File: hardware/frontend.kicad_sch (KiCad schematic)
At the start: 47 parts, among them J201 Conn_01x02, J202 Conn_01x02, J203 Conn_01x02, J204 Conn_01x02, J205 Conn_01x02, Q201 NPN, Q202 2N7002, U201 BQ7694204

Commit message: update schematics
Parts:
- removed R211: 1m, Resistor_SMD:R_1206_3216Metric, symbol Device:R_Small
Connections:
- net GND: no longer C204.2, C209.2, R212.2
- net PGND renamed PACK-
- net PACK-: now also C204.2
- new net BAT-: C209.2, R212.2
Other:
- note removed: "<-- Current --"

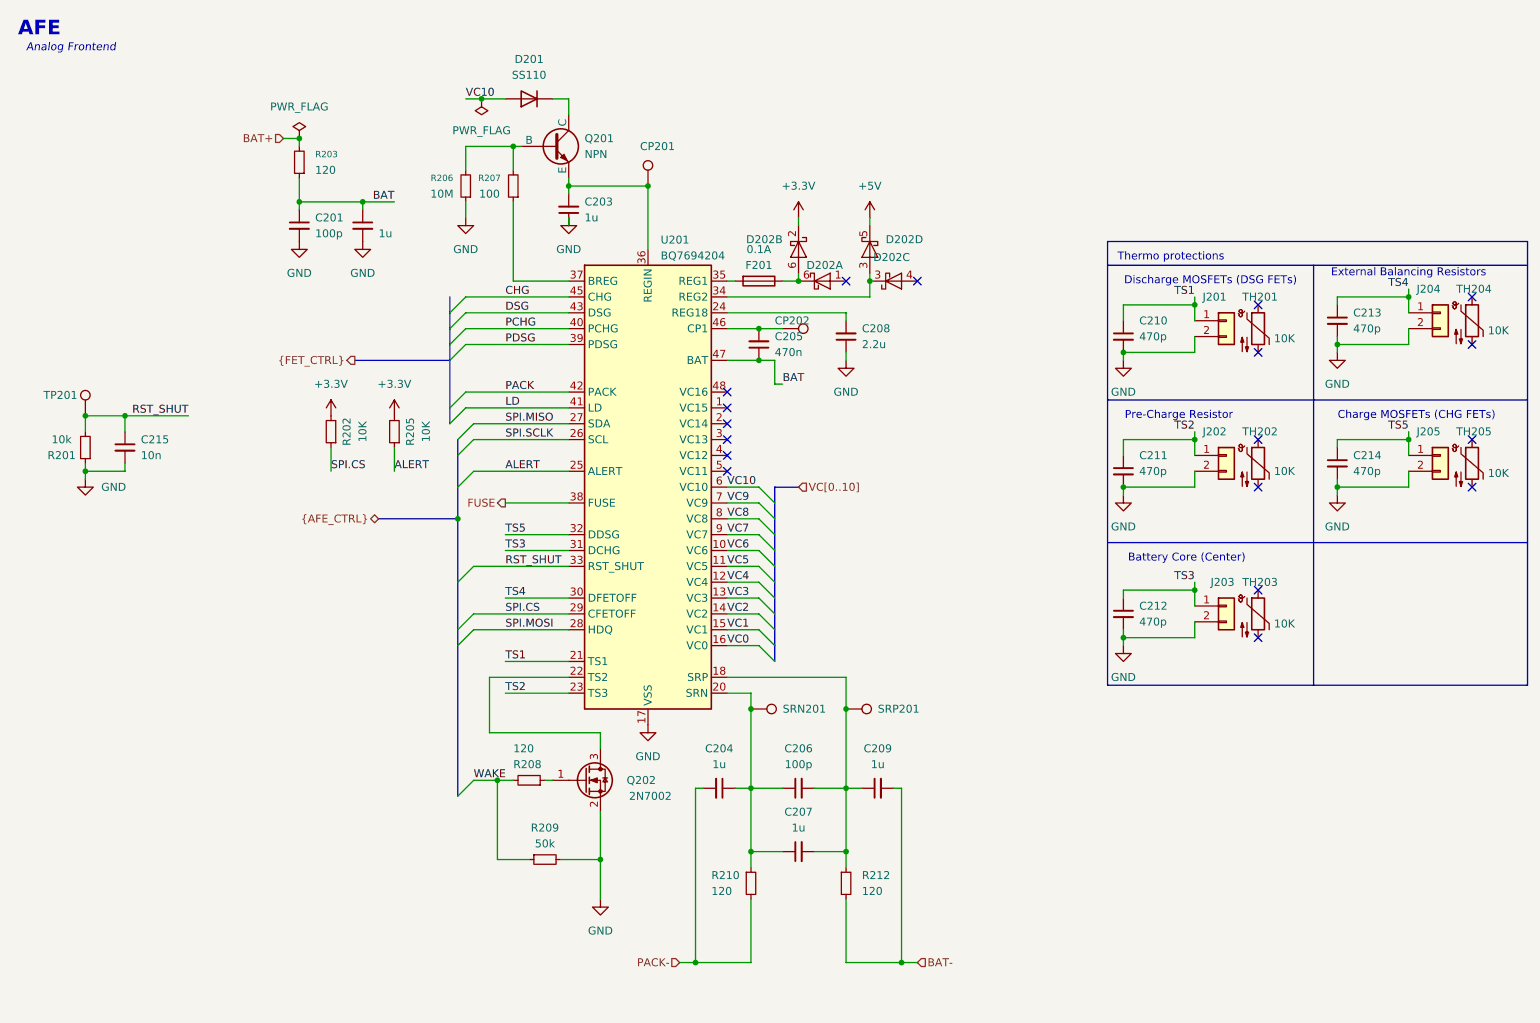
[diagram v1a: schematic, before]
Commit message: placed c mosfet
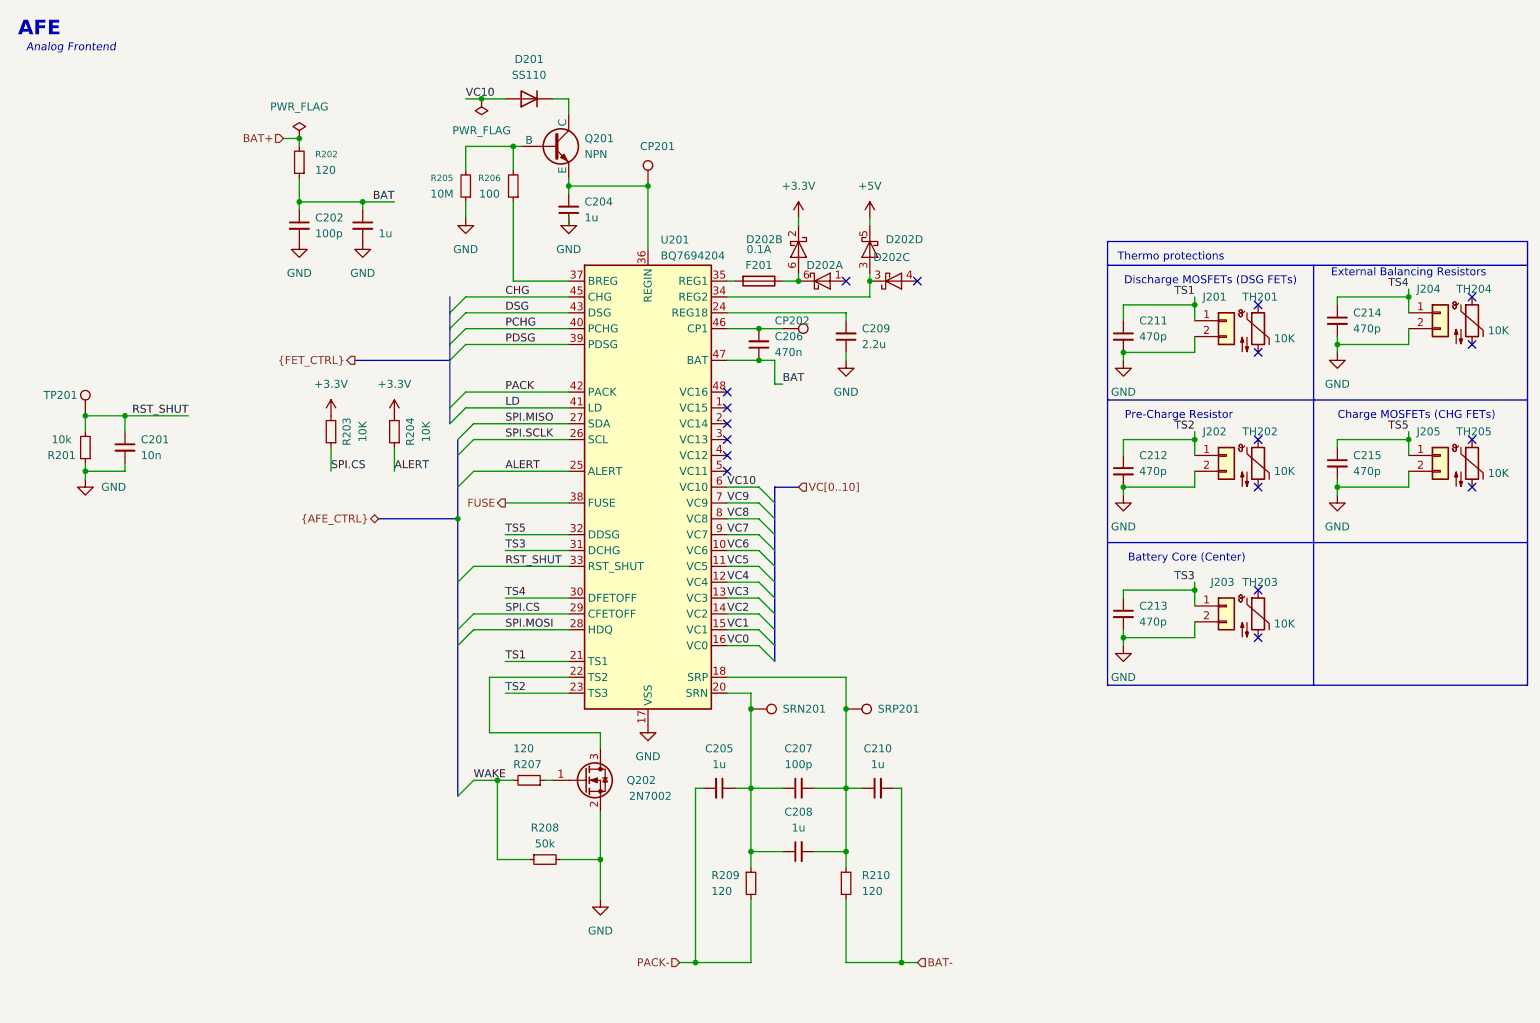
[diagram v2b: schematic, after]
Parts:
- C202: renamed from C201; footprint Capacitor_SMD:C_0805_2012Metric -> Capacitor_SMD:C_0603_1608Metric
- C204: renamed from C203; footprint Capacitor_SMD:C_0805_2012Metric -> Capacitor_SMD:C_0603_1608Metric
- C205: renamed from C204; footprint Capacitor_SMD:C_0805_2012Metric -> Capacitor_SMD:C_0603_1608Metric
- C206: renamed from C205; footprint Capacitor_SMD:C_0805_2012Metric -> Capacitor_SMD:C_0603_1608Metric
- C207: renamed from C206; footprint Capacitor_SMD:C_0805_2012Metric -> Capacitor_SMD:C_0603_1608Metric
- C208: renamed from C207; footprint Capacitor_SMD:C_0805_2012Metric -> Capacitor_SMD:C_0603_1608Metric
- C210: renamed from C209; footprint Capacitor_SMD:C_0805_2012Metric -> Capacitor_SMD:C_0603_1608Metric
- C211: renamed from C210; footprint Capacitor_SMD:C_0805_2012Metric -> Capacitor_SMD:C_0603_1608Metric
- C212: renamed from C211; footprint Capacitor_SMD:C_0805_2012Metric -> Capacitor_SMD:C_0603_1608Metric
- C213: renamed from C212; footprint Capacitor_SMD:C_0805_2012Metric -> Capacitor_SMD:C_0603_1608Metric
- C214: renamed from C213; footprint Capacitor_SMD:C_0805_2012Metric -> Capacitor_SMD:C_0603_1608Metric
- C215: renamed from C214; footprint Capacitor_SMD:C_0805_2012Metric -> Capacitor_SMD:C_0603_1608Metric
- R201: footprint Resistor_SMD:R_0805_2012Metric -> Resistor_SMD:R_0603_1608Metric
- R202: renamed from R203; footprint Resistor_SMD:R_0805_2012Metric -> Resistor_SMD:R_0603_1608Metric
- R203: renamed from R202; footprint Resistor_SMD:R_0805_2012Metric -> Resistor_SMD:R_0603_1608Metric
- R204: renamed from R205; footprint Resistor_SMD:R_0805_2012Metric -> Resistor_SMD:R_0603_1608Metric
- R205: renamed from R206; footprint Resistor_SMD:R_0805_2012Metric -> Resistor_SMD:R_0603_1608Metric
- R206: renamed from R207; footprint Resistor_SMD:R_0805_2012Metric -> Resistor_SMD:R_0603_1608Metric
- R207: renamed from R208; footprint Resistor_SMD:R_0805_2012Metric -> Resistor_SMD:R_0603_1608Metric
- R208: renamed from R209; footprint Resistor_SMD:R_0805_2012Metric -> Resistor_SMD:R_0603_1608Metric
- R209: renamed from R210; footprint Resistor_SMD:R_0805_2012Metric -> Resistor_SMD:R_0603_1608Metric
- R210: renamed from R212; footprint Resistor_SMD:R_0805_2012Metric -> Resistor_SMD:R_0603_1608Metric
- renumbered C215 to C201, C202 to C203, C208 to C209

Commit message: reduced BOM
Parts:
- C201: footprint (none) -> Capacitor_SMD:C_0603_1608Metric
- J201, J202, J203, J204, J205: footprint (none) -> Connector_Wire:SolderWire-0.15sqmm_1x02_P4mm_D0.5mm_OD1.5mm
- Q202: value 2N7002 -> DMG2302UK
- R203, R204: value 10K -> 10k
- R208: value 50k -> 49.9k
- TH201, TH202, TH203, TH204, TH205: value 10K -> 10k; footprint (none) -> Resistor_SMD:R_0603_1608Metric

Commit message: ADD ZONES
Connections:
- net BAT+ is gone; now on net VC10: R202.2
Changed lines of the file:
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@@
+	)
+	(junction
+		(at 35.56 83.82)
+		(diameter 0)
+		(color 0 0 0 0)
+	)
+	(junction
+		(at 143.51 62.23)
+		(diameter 0)
+		(color 0 0 0 0)
+	)
+	(junction
+		(at 207.01 66.04)
+		(diameter 0)
+		(color 0 0 0 0)
+	)
+	(junction
+		(at 195.58 73.66)
+		(diameter 0)
+		(color 0 0 0 0)
+	)
+	(junction
+		(at 135.89 143.51)
+		(diameter 0)
+		(color 0 0 0 0)
+	)
+	(junction
+		(at 241.3 87.63)
+		(diameter 0)
+		(color 0 0 0 0)
+	)
+	(junction
+		(at 195.58 95.25)
+		(diameter 0)
+		(color 0 0 0 0)
+	)
+	(junction
+		(at 97.79 40.64)
+		(diameter 0)
+		(color 0 0 0 0)
 	)
 	(junction
@@
 	)
 	(junction
-		(at 35.56 83.82)
-		(diameter 0)
-		(color 0 0 0 0)
-	)
-	(junction
-		(at 143.51 62.23)
-		(diameter 0)
-		(color 0 0 0 0)
-	)
-	(junction
-		(at 207.01 66.04)
-		(diameter 0)
-		(color 0 0 0 0)
-	)
-	(junction
-		(at 195.58 73.66)
-		(diameter 0)
-		(color 0 0 0 0)
-	)
-	(junction
-		(at 135.89 143.51)
-		(diameter 0)
-		(color 0 0 0 0)
-	)
-	(junction
-		(at 241.3 87.63)
-		(diameter 0)
-		(color 0 0 0 0)
-	)
-	(junction
-		(at 195.58 95.25)
-		(diameter 0)
-		(color 0 0 0 0)
-	)
-	(junction
-		(at 97.79 40.64)
-		(diameter 0)
-		(color 0 0 0 0)
-	)
-	(junction
 		(at 106.68 46.99)
 		(diameter 0)
@@
 	(wire
 		(pts
-			(xy 60.96 39.37) (xy 63.5 39.37)
+			(xy 57.15 39.37) (xy 63.5 39.37)
 		)
 		(stroke
@@
 	(label "VC7"
 		(at 132.08 102.87 0)
+		(effects
+			(font
+				(size 1.27 1.27)
+			)
+			(justify left bottom)
+		)
+	)
+	(label "VC10"
+		(at 57.15 39.37 0)
 		(effects
 			(font
@@
 		)
 	)
-	(hierarchical_label "BAT+"
-		(shape input)
-		(at 60.96 39.37 180)
-		(effects
-			(font
-				(size 1.27 1.27)
-			)
-			(justify right)
-		)
-	)

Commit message: some chnages
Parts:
- Q202: value DMG2302UK -> 2N7002K

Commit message: Replace huge SolderWire footprint with standard 2.54mm PinHeader
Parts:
- removed SRN201, SRP201: TestPoint, TestPoint:TestPoint_Pad_D1.0mm, symbol Connector:TestPoint
- J201, J202, J203, J204, J205: footprint Connector_Wire:SolderWire-0.15sqmm_1x02_P4mm_D0.5mm_OD1.5mm -> Connector_PinHeader_2.54mm:PinHeader_1x02_P2.54mm_Vertical
- TH201, TH202, TH203, TH204, TH205: now left out of the parts list
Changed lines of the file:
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@@
 	)
 	(junction
-		(at 151.13 130.81)
-		(diameter 0)
-		(color 0 0 0 0)
-	)
-	(junction
 		(at 137.16 69.85)
 		(diameter 0)
@@
 	)
 	(junction
-		(at 135.89 130.81)
-		(diameter 0)
-		(color 0 0 0 0)
-	)
-	(junction
 		(at 154.94 62.23)
 		(diameter 0)
@@
 		)
 	)
-	(wire
-		(pts
-			(xy 135.89 128.27) (xy 135.89 130.81)
-		)
-		(stroke
-			(width 0)
-			(type default)
-		)
-	)
 	(polyline
 		(pts
@@
 	(wire
 		(pts
-			(xy 151.13 125.73) (xy 151.13 130.81)
-		)
-		(stroke
-			(width 0)
-			(type default)
-		)
-	)
-	(wire
-		(pts
 			(xy 97.79 40.64) (xy 99.06 40.64)
 		)
@@
 	(wire
 		(pts
-			(xy 151.13 130.81) (xy 151.13 143.51)
+			(xy 151.13 125.73) (xy 151.13 143.51)
 		)
 		(stroke
@@
 	(wire
 		(pts
-			(xy 135.89 130.81) (xy 135.89 143.51)
+			(xy 135.89 128.27) (xy 135.89 143.51)
 		)
 		(stroke
@@
 		(body_style 1)
 		(exclude_from_sim no)
-		(in_bom yes)
-		(on_board yes)
-		(in_pos_files yes)
+		(in_bom no)
+		(on_board no)
+		(in_pos_files no)
 		(dnp no)
 		(property "Reference" "TH204"
@@
 			)
 		)
-		(property "Footprint" "Connector_Wire:SolderWire-0.15sqmm_1x02_P4mm_D0.5mm_OD1.5mm"
+		(property "Footprint" "Connector_PinHeader_2.54mm:PinHeader_1x02_P2.54mm_Vertical"
 			(at 212.09 114.3 0)
 			(hide yes)
@@
 		(body_style 1)
 		(exclude_from_sim no)
-		(in_bom yes)
-		(on_board yes)
-		(in_pos_files yes)
+		(in_bom no)
+		(on_board no)
+		(in_pos_files no)
 		(dnp no)
 		(property "Reference" "TH201"
@@
 			)
 		)
-		(property "Footprint" "Connector_Wire:SolderWire-0.15sqmm_1x02_P4mm_D0.5mm_OD1.5mm"
+		(property "Footprint" "Connector_PinHeader_2.54mm:PinHeader_1x02_P2.54mm_Vertical"
 			(at 246.38 67.31 0)
 			(hide yes)
@@
 			)
 		)
-		(property "Footprint" "Connector_Wire:SolderWire-0.15sqmm_1x02_P4mm_D0.5mm_OD1.5mm"
+		(property "Footprint" "Connector_PinHeader_2.54mm:PinHeader_1x02_P2.54mm_Vertical"
 			(at 212.09 68.58 0)
 			(hide yes)
@@
 	)
 	(symbol
-		(lib_id "Connector:TestPoint")
-		(at 135.89 130.81 270)
-		(unit 1)
-		(body_style 1)
-		(exclude_from_sim no)
-		(in_bom yes)
-		(on_board yes)
-		(in_pos_files yes)
-		(dnp no)
-		(property "Reference" "SRN201"
-			(at 140.97 130.81 90)
-			(show_name no)
-			(do_not_autoplace no)
-			(effects
-				(font
-					(size 1.27 1.27)
-				)
-				(justify left)
-			)
-		)
-		(property "Value" "TestPoint"
-			(at 137.9221 133.35 0)
-			(hide yes)
-			(show_name no)
-			(do_not_autoplace no)
-			(effects
-				(font
-					(size 1.27 1.27)
-				)
-				(justify left)
-			)
-		)
-		(property "Footprint" "TestPoint:TestPoint_Pad_D1.0mm"
-			(at 135.89 135.89 0)
-			(hide yes)
-			(show_name no)
-			(do_not_autoplace no)
-			(effects
-				(font
-					(size 1.27 1.27)
-				)
-			)
-		)
-		(property "Datasheet" ""
-			(at 135.89 135.89 0)
-			(hide yes)
-			(show_name no)
-			(do_not_autoplace no)
-			(effects
-				(font
-					(size 1.27 1.27)
-				)
-			)
-		)
-		(property "Description" "test point"
-			(at 135.89 130.81 0)
-			(hide yes)
-			(show_name no)
-			(do_not_autoplace no)
-			(effects
-				(font
-					(size 1.27 1.27)
-				)
-			)
-		)
-		(pin "1"
-		)
-		(instances
-			(project "wafel-eval-board"
-				(path "/3e668e3e-3e16-4665-a807-4735962c41d3/204526d9-bdaf-4b36-9252-b50630c4791c"
-					(reference "SRN201")
-					(unit 1)
-				)
-			)
-		)
-	)
-	(symbol
 		(lib_id "Diode:BAT54SDW")
 		(at 158.75 62.23 0)
@@
 			)
 		)
-		(property "Footprint" "Connector_Wire:SolderWire-0.15sqmm_1x02_P4mm_D0.5mm_OD1.5mm"
+		(property "Footprint" "Connector_PinHeader_2.54mm:PinHeader_1x02_P2.54mm_Vertical"
 			(at 246.38 90.17 0)
 			(hide yes)
@@
 		(body_style 1)
 		(exclude_from_sim no)
-		(in_bom yes)
-		(on_board yes)
-		(in_pos_files yes)
+		(in_bom no)
+		(on_board no)
+		(in_pos_files no)
 		(dnp no)
 		(property "Reference" "TH203"
@@
 	)
 	(symbol
-		(lib_id "Connector:TestPoint")
-		(at 151.13 130.81 270)
-		(unit 1)
-		(body_style 1)
-		(exclude_from_sim no)
-		(in_bom yes)
-		(on_board yes)
-		(in_pos_files yes)
-		(dnp no)
-		(property "Reference" "SRP201"
-			(at 156.21 130.81 90)
-			(show_name no)
-			(do_not_autoplace no)
-			(effects
-				(font
-					(size 1.27 1.27)
-				)
-				(justify left)
-			)
-		)
-		(property "Value" "TestPoint"
-			(at 153.1621 133.35 0)
-			(hide yes)
-			(show_name no)
-			(do_not_autoplace no)
-			(effects
-				(font
-					(size 1.27 1.27)
-				)
-				(justify left)
-			)
-		)
-		(property "Footprint" "TestPoint:TestPoint_Pad_D1.0mm"
-			(at 151.13 135.89 0)
-			(hide yes)
-			(show_name no)
-			(do_not_autoplace no)
-			(effects
-				(font
-					(size 1.27 1.27)
-				)
-			)
-		)
-		(property "Datasheet" ""
-			(at 151.13 135.89 0)
-			(hide yes)
-			(show_name no)
-			(do_not_autoplace no)
-			(effects
-				(font
-					(size 1.27 1.27)
-				)
-			)
-		)
-		(property "Description" "test point"
-			(at 151.13 130.81 0)
-			(hide yes)
-			(show_name no)
-			(do_not_autoplace no)
-			(effects
-				(font
-					(size 1.27 1.27)
-				)
-			)
-		)
-		(pin "1"
-		)
-		(instances
-			(project "frontend"
-				(path "/00a1254e-6313-43f2-bc4f-c22473deb189"
-					(reference "SRP101")
-					(unit 1)
-				)
-			)
-			(project "wafel-eval-board"
-				(path "/3e668e3e-3e16-4665-a807-4735962c41d3/204526d9-bdaf-4b36-9252-b50630c4791c"
-					(reference "SRP201")
-					(unit 1)
-				)
-			)
-		)
-	)
-	(symbol
 		(lib_id "Simulation_SPICE:NPN")
 		(at 104.14 40.64 0)
@@
 		(body_style 1)
 		(exclude_from_sim no)
-		(in_bom yes)
-		(on_board yes)
-		(in_pos_files yes)
+		(in_bom no)
+		(on_board no)
+		(in_pos_files no)
 		(dnp no)
 		(property "Reference" "TH202"
@@
 			)
 		)
-		(property "Footprint" "Connector_Wire:SolderWire-0.15sqmm_1x02_P4mm_D0.5mm_OD1.5mm"
+		(property "Footprint" "Connector_PinHeader_2.54mm:PinHeader_1x02_P2.54mm_Vertical"
 			(at 212.09 90.17 0)
 			(hide yes)
@@
 		(body_style 1)
 		(exclude_from_sim no)
-		(in_bom yes)
-		(on_board yes)
-		(in_pos_files yes)
+		(in_bom no)
+		(on_board no)
+		(in_pos_files no)
 		(dnp no)
 		(property "Reference" "TH205"
